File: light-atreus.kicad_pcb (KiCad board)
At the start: 2 copper layers, 37.4 x 44.1 mm, 4 parts, among them J1 USB_OTG, J4 USB_OTG

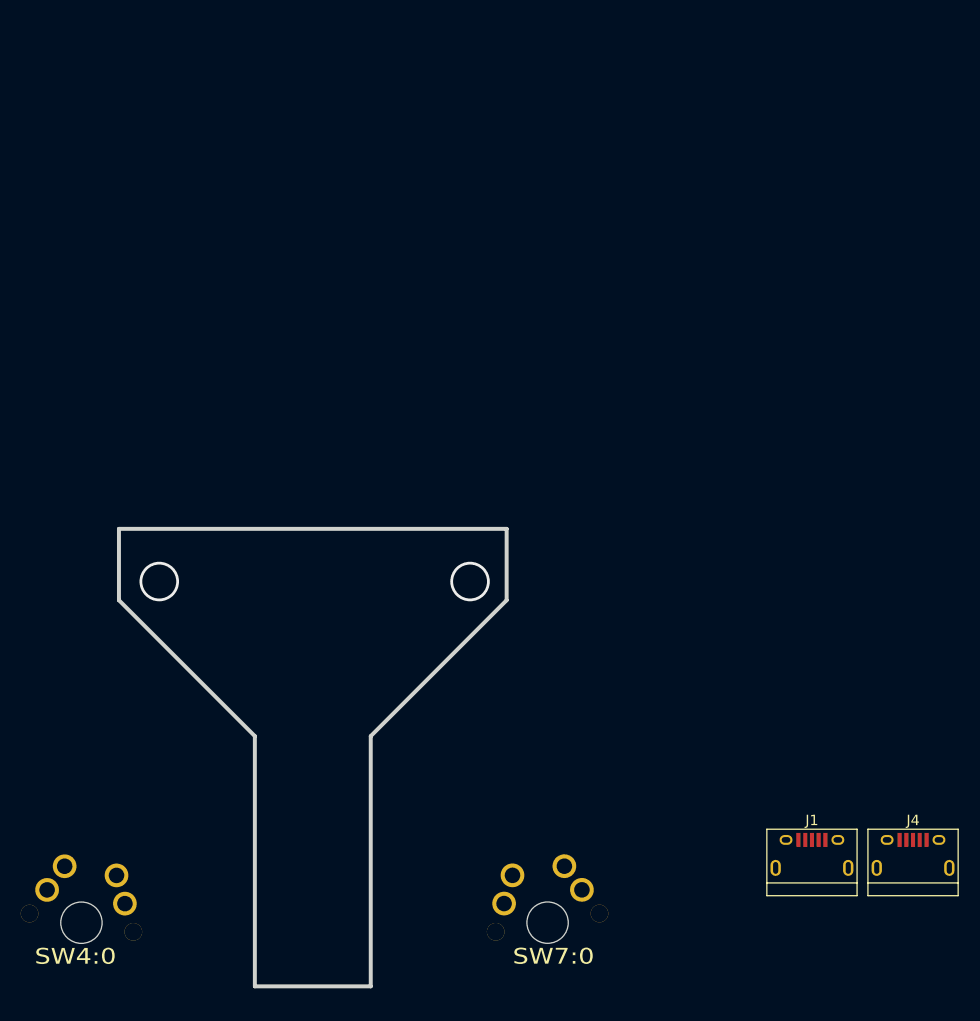
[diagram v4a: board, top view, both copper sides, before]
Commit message: Roughly place footprints for solder points on board
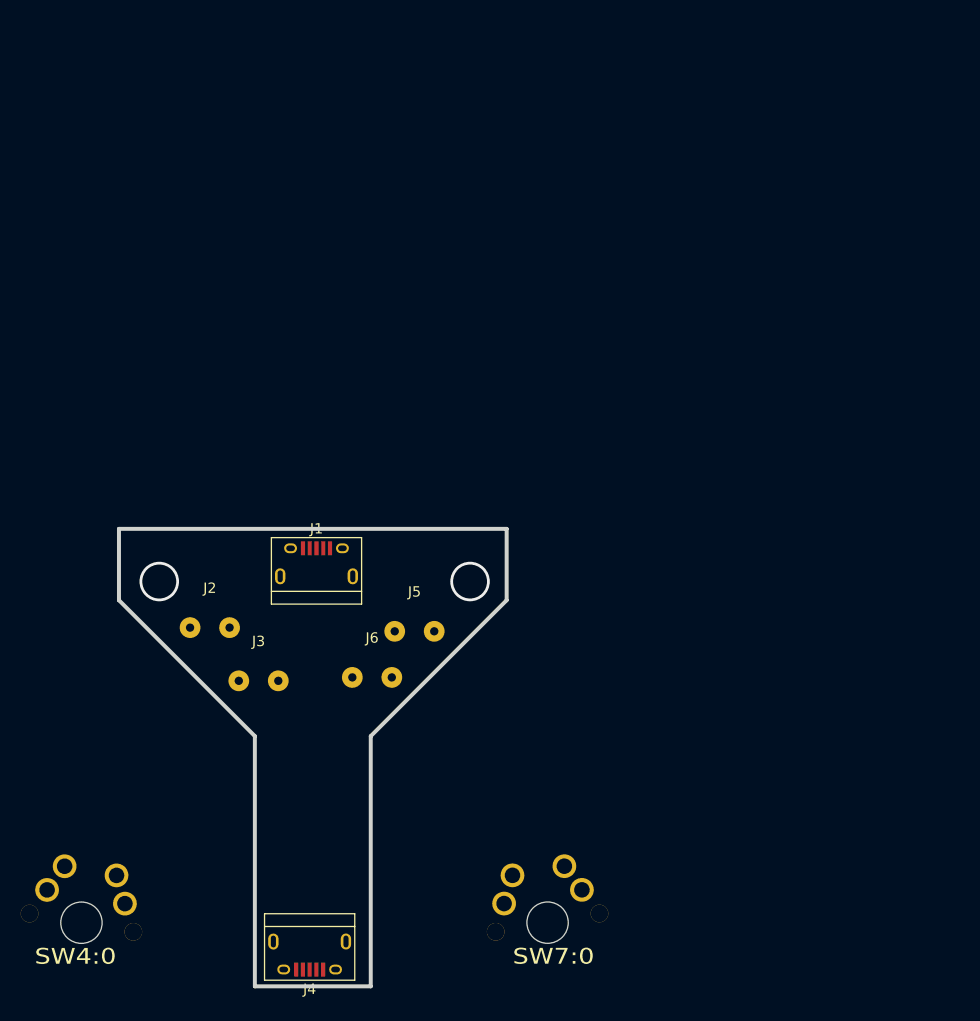
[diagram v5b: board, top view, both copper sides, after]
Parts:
- added J2: CONN_01X02, custom_footprints:SolderWirePad_1x2-8mm, F.Cu at (122.7, 99.3)
- added J3: CONN_01X02, custom_footprints:SolderWirePad_1x2-8mm, F.Cu at (127.4, 104.4)
- added J5: CONN_01X02, custom_footprints:SolderWirePad_1x2-8mm, F.Cu at (142.4, 99.6)
- added J6: CONN_01X02, custom_footprints:SolderWirePad_1x2-8mm, F.Cu at (138.3, 104.1)
- moved J4 59.0 mm to (132.3, 130.9), turned to 180 degrees
- moved J1 55.4 mm to (132.9, 93.0)
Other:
- net class Default: clearance 0.254 -> 0
- rule trace_clearance: 0.254 -> 0
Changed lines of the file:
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@@
     (tracks 2)
     (zones 0)
-    (modules 4)
-    (nets 11)
+    (modules 8)
+    (nets 15)
   )
   (page A4)
@@
   (setup
     (last_trace_width 0.2032)
-    (trace_clearance 0.254)
+    (trace_clearance 0)
     (zone_clearance 0.508)
     (zone_45_only no)
@@
   (net 9 "Net-(J1-Pad2)")
   (net 10 "Net-(J1-Pad1)")
+  (net 11 "Net-(J2-Pad2)")
+  (net 12 "Net-(J3-Pad2)")
+  (net 13 "Net-(J5-Pad2)")
+  (net 14 "Net-(J6-Pad2)")
   (net_class Default "This is the default net class."
-    (clearance 0.254)
+    (clearance 0)
     (trace_width 0.2032)
     (via_dia 0.889)
@@
     (add_net "Net-(J1-Pad5)")
     (add_net "Net-(J1-Pad6)")
+    (add_net "Net-(J2-Pad2)")
+    (add_net "Net-(J3-Pad2)")
+    (add_net "Net-(J5-Pad2)")
+    (add_net "Net-(J6-Pad2)")
   )
   (module MX_FLIP locked (layer Front)
@@
   )
   (module Connectors:USB_Micro-B (layer Front)
-    (at 180.723742 121.085187)
+    (at 132.9436 92.964)
     (descr "Micro USB Type B Receptacle")
     (tags "USB USB_B USB_micro USB_OTG")
@@
   )
   (module Connectors:USB_Micro-B (layer Front)
-    (at 190.473742 121.085187)
+    (at 132.2832 130.8862 180)
     (descr "Micro USB Type B Receptacle")
     (tags "USB USB_B USB_micro USB_OTG")
     (attr smd)
-    (fp_text reference J4 (at 0 -3.24) (layer F.SilkS)
-      (effects (font (size 1 1) (thickness 0.15)))
-    )
-    (fp_text value USB_OTG (at 0 5.01) (layer F.Fab)
+    (fp_text reference J4 (at 0 -3.24 180) (layer F.SilkS)
+      (effects (font (size 1 1) (thickness 0.15)))
+    )
+    (fp_text value USB_OTG (at 0 5.01 180) (layer F.Fab)
       (effects (font (size 1 1) (thickness 0.15)))
     )
@@
     (fp_line (start 4.35 2.8) (end -4.35 2.8) (layer F.SilkS) (width 0.12))
     (fp_line (start -4.35 4.03) (end -4.35 -2.38) (layer F.SilkS) (width 0.12))
-    (pad 1 smd rect (at -1.3 -1.35 90) (size 1.35 0.4) (layers Front F.Paste F.Mask)
-      (net 10 "Net-(J1-Pad1)"))
-    (pad 2 smd rect (at -0.65 -1.35 90) (size 1.35 0.4) (layers Front F.Paste F.Mask)
+    (pad 1 smd rect (at -1.3 -1.35 270) (size 1.35 0.4) (layers Front F.Paste F.Mask)
+      (net 10 "Net-(J1-Pad1)"))
+    (pad 2 smd rect (at -0.65 -1.35 270) (size 1.35 0.4) (layers Front F.Paste F.Mask)
       (net 9 "Net-(J1-Pad2)"))
-    (pad 3 smd rect (at 0 -1.35 90) (size 1.35 0.4) (layers Front F.Paste F.Mask)
+    (pad 3 smd rect (at 0 -1.35 270) (size 1.35 0.4) (layers Front F.Paste F.Mask)
       (net 8 "Net-(J1-Pad3)"))
-    (pad 4 smd rect (at 0.65 -1.35 90) (size 1.35 0.4) (layers Front F.Paste F.Mask)
+    (pad 4 smd rect (at 0.65 -1.35 270) (size 1.35 0.4) (layers Front F.Paste F.Mask)
       (net 7 "Net-(J1-Pad4)"))
-    (pad 5 smd rect (at 1.3 -1.35 90) (size 1.35 0.4) (layers Front F.Paste F.Mask)
-      (net 6 "Net-(J1-Pad5)"))
-    (pad 6 thru_hole oval (at -2.5 -1.35 90) (size 0.95 1.25) (drill oval 0.55 0.85) (layers *.Cu *.Mask)
-      (net 5 "Net-(J1-Pad6)"))
-    (pad 6 thru_hole oval (at 2.5 -1.35 90) (size 0.95 1.25) (drill oval 0.55 0.85) (layers *.Cu *.Mask)
-      (net 5 "Net-(J1-Pad6)"))
-    (pad 6 thru_hole oval (at -3.5 1.35 90) (size 1.55 1) (drill oval 1.15 0.5) (layers *.Cu *.Mask)
-      (net 5 "Net-(J1-Pad6)"))
-    (pad 6 thru_hole oval (at 3.5 1.35 90) (size 1.55 1) (drill oval 1.15 0.5) (layers *.Cu *.Mask)
-      (net 5 "Net-(J1-Pad6)"))
+    (pad 5 smd rect (at 1.3 -1.35 270) (size 1.35 0.4) (layers Front F.Paste F.Mask)
+      (net 6 "Net-(J1-Pad5)"))
+    (pad 6 thru_hole oval (at -2.5 -1.35 270) (size 0.95 1.25) (drill oval 0.55 0.85) (layers *.Cu *.Mask)
+      (net 5 "Net-(J1-Pad6)"))
+    (pad 6 thru_hole oval (at 2.5 -1.35 270) (size 0.95 1.25) (drill oval 0.55 0.85) (layers *.Cu *.Mask)
+      (net 5 "Net-(J1-Pad6)"))
+    (pad 6 thru_hole oval (at -3.5 1.35 270) (size 1.55 1) (drill oval 1.15 0.5) (layers *.Cu *.Mask)
+      (net 5 "Net-(J1-Pad6)"))
+    (pad 6 thru_hole oval (at 3.5 1.35 270) (size 1.55 1) (drill oval 1.15 0.5) (layers *.Cu *.Mask)
+      (net 5 "Net-(J1-Pad6)"))
+  )
+  (module custom_footprints:SolderWirePad_1x2-8mm (layer Front)
+    (at 122.6566 99.2632)
+    (fp_text reference J2 (at 0 -3.81) (layer F.SilkS)
+      (effects (font (size 1 1) (thickness 0.15)))
+    )
+    (fp_text value CONN_01X02 (at 0.635 2.54) (layer F.Fab)
+      (effects (font (size 1 1) (thickness 0.15)))
+    )
+    (pad 2 thru_hole circle (at 1.905 0) (size 1.99898 1.99898) (drill 0.8001) (layers *.Cu *.Mask)
+      (net 11 "Net-(J2-Pad2)"))
+    (pad 1 thru_hole circle (at -1.905 0) (size 1.99898 1.99898) (drill 0.8001) (layers *.Cu *.Mask)
+      (net 10 "Net-(J1-Pad1)"))
+  )
+  (module custom_footprints:SolderWirePad_1x2-8mm (layer Front)
+    (at 127.3556 104.394)
+    (fp_text reference J3 (at 0 -3.81) (layer F.SilkS)
+      (effects (font (size 1 1) (thickness 0.15)))
+    )
+    (fp_text value CONN_01X02 (at 0.635 2.54) (layer F.Fab)
+      (effects (font (size 1 1) (thickness 0.15)))
+    )
+    (pad 1 thru_hole circle (at -1.905 0) (size 1.99898 1.99898) (drill 0.8001) (layers *.Cu *.Mask)
+      (net 6 "Net-(J1-Pad5)"))
+    (pad 2 thru_hole circle (at 1.905 0) (size 1.99898 1.99898) (drill 0.8001) (layers *.Cu *.Mask)
+      (net 12 "Net-(J3-Pad2)"))
+  )
+  (module custom_footprints:SolderWirePad_1x2-8mm (layer Front)
+    (at 142.3924 99.6188)
+    (fp_text reference J5 (at 0 -3.81) (layer F.SilkS)
+      (effects (font (size 1 1) (thickness 0.15)))
+    )
+    (fp_text value CONN_01X02 (at 0.635 2.54) (layer F.Fab)
+      (effects (font (size 1 1) (thickness 0.15)))
+    )
+    (pad 2 thru_hole circle (at 1.905 0) (size 1.99898 1.99898) (drill 0.8001) (layers *.Cu *.Mask)
+      (net 13 "Net-(J5-Pad2)"))
+    (pad 1 thru_hole circle (at -1.905 0) (size 1.99898 1.99898) (drill 0.8001) (layers *.Cu *.Mask)
+      (net 10 "Net-(J1-Pad1)"))
+  )
+  (module custom_footprints:SolderWirePad_1x2-8mm (layer Front)
+    (at 138.303 104.0638)
+    (fp_text reference J6 (at 0 -3.81) (layer F.SilkS)
+      (effects (font (size 1 1) (thickness 0.15)))
+    )
+    (fp_text value CONN_01X02 (at 0.635 2.54) (layer F.Fab)
+      (effects (font (size 1 1) (thickness 0.15)))
+    )
+    (pad 1 thru_hole circle (at -1.905 0) (size 1.99898 1.99898) (drill 0.8001) (layers *.Cu *.Mask)
+      (net 6 "Net-(J1-Pad5)"))
+    (pad 2 thru_hole circle (at 1.905 0) (size 1.99898 1.99898) (drill 0.8001) (layers *.Cu *.Mask)
+      (net 14 "Net-(J6-Pad2)"))
   )
   (gr_line (start 151.2824 96.6216) (end 138.176 109.728) (layer Edge.Cuts) (width 0.381))

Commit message: Name nets on broken out pins
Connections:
- net Net-(J1-Pad1) renamed /VBUS
- net Net-(J1-Pad5) renamed /GND
- J2 pad 2: Net-(J2-Pad2) -> (no net)
- J3 pad 2: Net-(J3-Pad2) -> (no net)
- J5 pad 2: Net-(J5-Pad2) -> (no net)
- J6 pad 2: Net-(J6-Pad2) -> (no net)
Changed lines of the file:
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@@
     (zones 0)
     (modules 8)
-    (nets 15)
+    (nets 11)
   )
   (page A4)
@@
   (net 4 N-diode-28)
   (net 5 "Net-(J1-Pad6)")
-  (net 6 "Net-(J1-Pad5)")
-  (net 7 "Net-(J1-Pad4)")
-  (net 8 "Net-(J1-Pad3)")
-  (net 9 "Net-(J1-Pad2)")
-  (net 10 "Net-(J1-Pad1)")
-  (net 11 "Net-(J2-Pad2)")
-  (net 12 "Net-(J3-Pad2)")
-  (net 13 "Net-(J5-Pad2)")
-  (net 14 "Net-(J6-Pad2)")
+  (net 6 "Net-(J1-Pad4)")
+  (net 7 "Net-(J1-Pad3)")
+  (net 8 "Net-(J1-Pad2)")
+  (net 9 /GND)
+  (net 10 /VBUS)
   (net_class Default "This is the default net class."
     (clearance 0)
@@
     (uvia_dia 0.508)
     (uvia_drill 0.127)
+    (add_net /GND)
+    (add_net /VBUS)
     (add_net N-col-4)
     (add_net N-col-6)
     (add_net N-diode-16)
     (add_net N-diode-28)
-    (add_net "Net-(J1-Pad1)")
     (add_net "Net-(J1-Pad2)")
     (add_net "Net-(J1-Pad3)")
     (add_net "Net-(J1-Pad4)")
-    (add_net "Net-(J1-Pad5)")
     (add_net "Net-(J1-Pad6)")
-    (add_net "Net-(J2-Pad2)")
-    (add_net "Net-(J3-Pad2)")
-    (add_net "Net-(J5-Pad2)")
-    (add_net "Net-(J6-Pad2)")
   )
   (module MX_FLIP locked (layer Front)
@@
       (net 5 "Net-(J1-Pad6)"))
     (pad 5 smd rect (at 1.3 -1.35 90) (size 1.35 0.4) (layers Front F.Paste F.Mask)
-      (net 6 "Net-(J1-Pad5)"))
+      (net 9 /GND))
     (pad 4 smd rect (at 0.65 -1.35 90) (size 1.35 0.4) (layers Front F.Paste F.Mask)
-      (net 7 "Net-(J1-Pad4)"))
+      (net 6 "Net-(J1-Pad4)"))
     (pad 3 smd rect (at 0 -1.35 90) (size 1.35 0.4) (layers Front F.Paste F.Mask)
-      (net 8 "Net-(J1-Pad3)"))
+      (net 7 "Net-(J1-Pad3)"))
     (pad 2 smd rect (at -0.65 -1.35 90) (size 1.35 0.4) (layers Front F.Paste F.Mask)
-      (net 9 "Net-(J1-Pad2)"))
+      (net 8 "Net-(J1-Pad2)"))
     (pad 1 smd rect (at -1.3 -1.35 90) (size 1.35 0.4) (layers Front F.Paste F.Mask)
-      (net 10 "Net-(J1-Pad1)"))
+      (net 10 /VBUS))
   )
   (module Connectors:USB_Micro-B (layer Front)
@@
     (fp_line (start -4.35 4.03) (end -4.35 -2.38) (layer F.SilkS) (width 0.12))
     (pad 1 smd rect (at -1.3 -1.35 270) (size 1.35 0.4) (layers Front F.Paste F.Mask)
-      (net 10 "Net-(J1-Pad1)"))
+      (net 10 /VBUS))
     (pad 2 smd rect (at -0.65 -1.35 270) (size 1.35 0.4) (layers Front F.Paste F.Mask)
-      (net 9 "Net-(J1-Pad2)"))
+      (net 8 "Net-(J1-Pad2)"))
     (pad 3 smd rect (at 0 -1.35 270) (size 1.35 0.4) (layers Front F.Paste F.Mask)
-      (net 8 "Net-(J1-Pad3)"))
+      (net 7 "Net-(J1-Pad3)"))
     (pad 4 smd rect (at 0.65 -1.35 270) (size 1.35 0.4) (layers Front F.Paste F.Mask)
-      (net 7 "Net-(J1-Pad4)"))
+      (net 6 "Net-(J1-Pad4)"))
     (pad 5 smd rect (at 1.3 -1.35 270) (size 1.35 0.4) (layers Front F.Paste F.Mask)
-      (net 6 "Net-(J1-Pad5)"))
+      (net 9 /GND))
     (pad 6 thru_hole oval (at -2.5 -1.35 270) (size 0.95 1.25) (drill oval 0.55 0.85) (layers *.Cu *.Mask)
       (net 5 "Net-(J1-Pad6)"))
@@
       (effects (font (size 1 1) (thickness 0.15)))
     )
-    (pad 2 thru_hole circle (at 1.905 0) (size 1.99898 1.99898) (drill 0.8001) (layers *.Cu *.Mask)
-      (net 11 "Net-(J2-Pad2)"))
-    (pad 1 thru_hole circle (at -1.905 0) (size 1.99898 1.99898) (drill 0.8001) (layers *.Cu *.Mask)
-      (net 10 "Net-(J1-Pad1)"))
+    (pad 2 thru_hole circle (at 1.905 0) (size 1.99898 1.99898) (drill 0.8001) (layers *.Cu *.Mask))
+    (pad 1 thru_hole circle (at -1.905 0) (size 1.99898 1.99898) (drill 0.8001) (layers *.Cu *.Mask)
+      (net 10 /VBUS))
   )
   (module custom_footprints:SolderWirePad_1x2-8mm (layer Front)
@@
     )
     (pad 1 thru_hole circle (at -1.905 0) (size 1.99898 1.99898) (drill 0.8001) (layers *.Cu *.Mask)
-      (net 6 "Net-(J1-Pad5)"))
-    (pad 2 thru_hole circle (at 1.905 0) (size 1.99898 1.99898) (drill 0.8001) (layers *.Cu *.Mask)
-      (net 12 "Net-(J3-Pad2)"))
+      (net 9 /GND))
+    (pad 2 thru_hole circle (at 1.905 0) (size 1.99898 1.99898) (drill 0.8001) (layers *.Cu *.Mask))
   )
   (module custom_footprints:SolderWirePad_1x2-8mm (layer Front)
@@
       (effects (font (size 1 1) (thickness 0.15)))
     )
-    (pad 2 thru_hole circle (at 1.905 0) (size 1.99898 1.99898) (drill 0.8001) (layers *.Cu *.Mask)
-      (net 13 "Net-(J5-Pad2)"))
-    (pad 1 thru_hole circle (at -1.905 0) (size 1.99898 1.99898) (drill 0.8001) (layers *.Cu *.Mask)
-      (net 10 "Net-(J1-Pad1)"))
+    (pad 2 thru_hole circle (at 1.905 0) (size 1.99898 1.99898) (drill 0.8001) (layers *.Cu *.Mask))
+    (pad 1 thru_hole circle (at -1.905 0) (size 1.99898 1.99898) (drill 0.8001) (layers *.Cu *.Mask)
+      (net 10 /VBUS))
   )
   (module custom_footprints:SolderWirePad_1x2-8mm (layer Front)
@@
     )
     (pad 1 thru_hole circle (at -1.905 0) (size 1.99898 1.99898) (drill 0.8001) (layers *.Cu *.Mask)
-      (net 6 "Net-(J1-Pad5)"))
-    (pad 2 thru_hole circle (at 1.905 0) (size 1.99898 1.99898) (drill 0.8001) (layers *.Cu *.Mask)
-      (net 14 "Net-(J6-Pad2)"))
+      (net 9 /GND))
+    (pad 2 thru_hole circle (at 1.905 0) (size 1.99898 1.99898) (drill 0.8001) (layers *.Cu *.Mask))
   )
   (gr_line (start 151.2824 96.6216) (end 138.176 109.728) (layer Edge.Cuts) (width 0.381))
